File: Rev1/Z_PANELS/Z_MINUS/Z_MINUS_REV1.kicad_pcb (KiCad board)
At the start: 2 copper layers, 98 x 98 mm, 57 parts, among them IC1 LTC4316IDD#PBF, IC2 SM141K08TFV, IC3 SM141K04TFV, IC4 SM141K04TFV, IC5 SM141K04TFV, IC6 SM141K08TFV, J1 F3311A7H121014E200, Q1 BSS138, Q2 BSS138, Q3 MBT2222ADW1T1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

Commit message: fixed bugs and finished Z plus
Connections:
- JP2 pad 3: /SUN_SENSOR/+3.3v -> +3.3V
- U1 pad 1: /SUN_SENSOR/+3.3v -> +3.3V
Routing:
- net +3.3V: track 144.2 -> 157.6 mm
- net /SUN_SENSOR/+3.3v: track 2.25 -> 0.00 mm

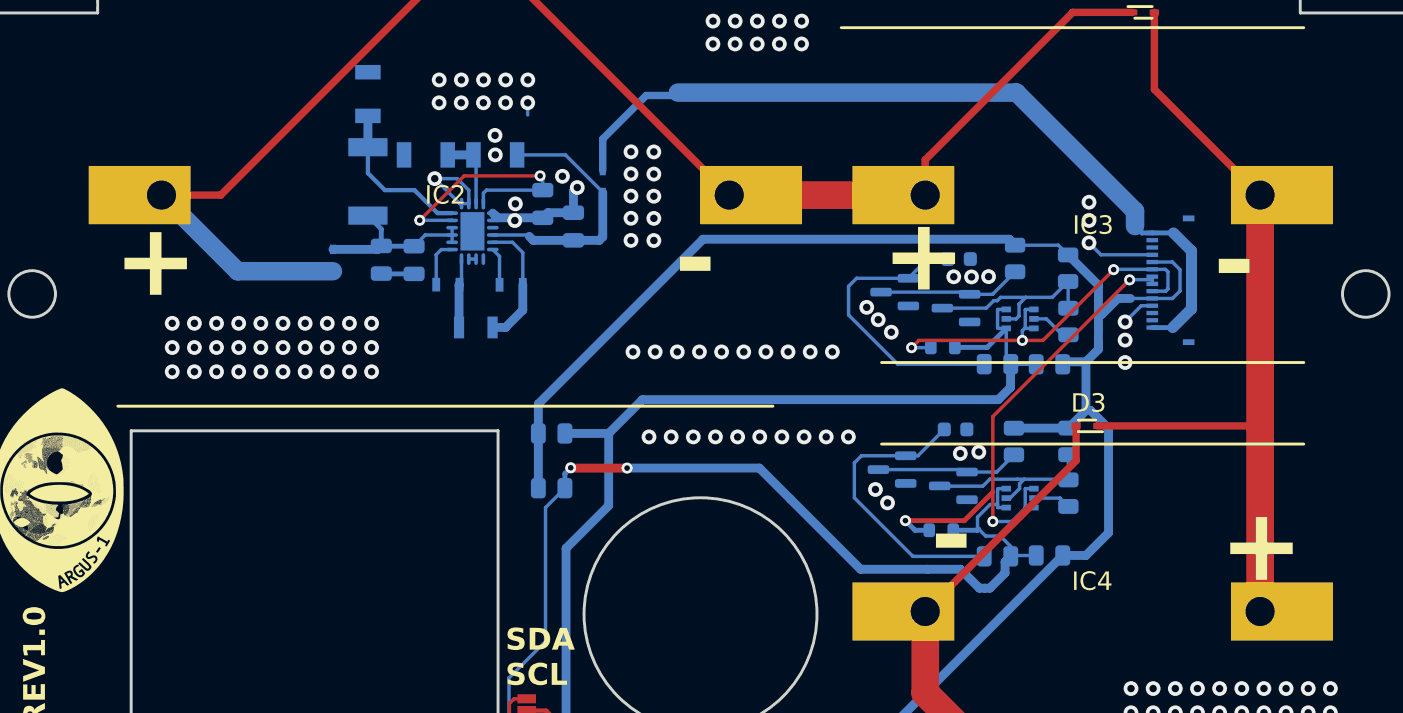
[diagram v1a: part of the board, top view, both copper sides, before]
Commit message: CHANGED Resistor values for MPPC; added testpoints and silkscreen info
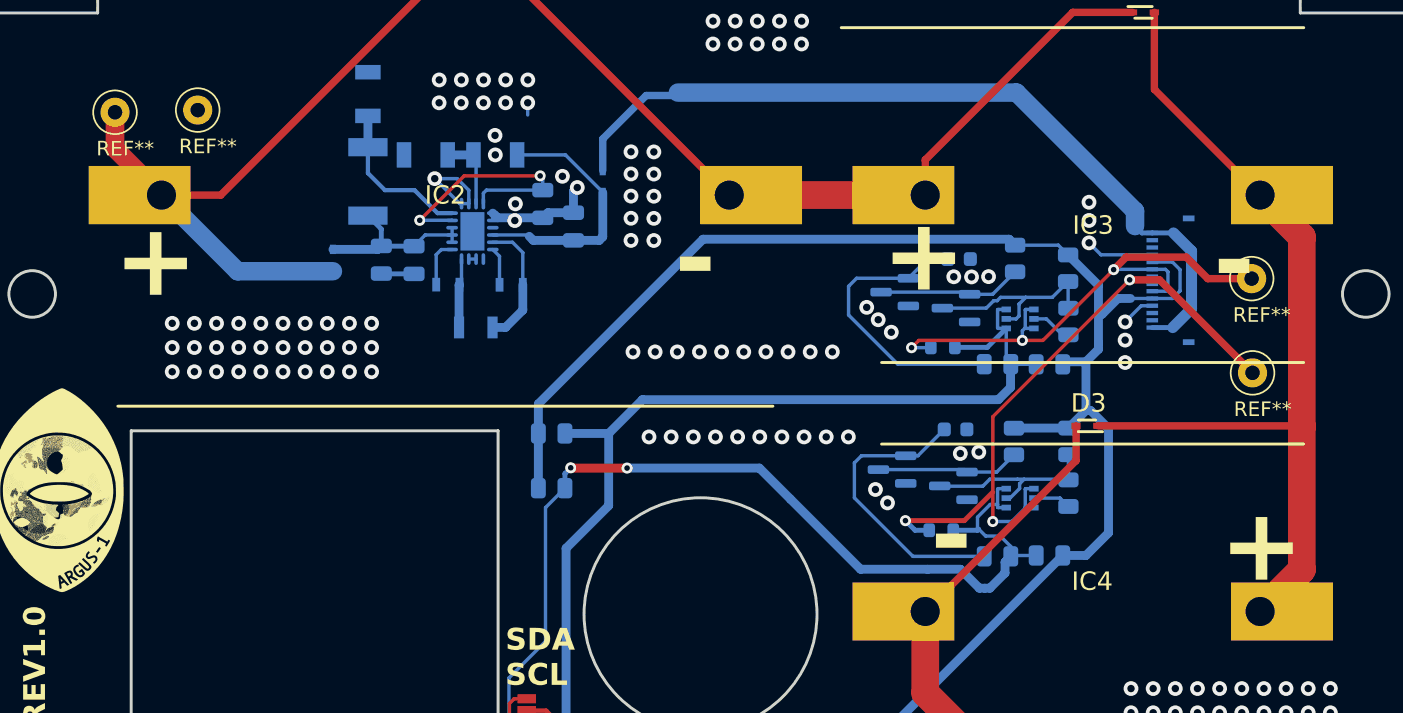
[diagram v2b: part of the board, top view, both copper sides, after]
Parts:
- added REF**: TestPoint_Loop_D2.50mm_Drill1.0mm, TestPoint:TestPoint_Loop_D2.50mm_Drill1.0mm, F.Cu at (102.0, 67.0)
- added REF**: TestPoint_Loop_D2.50mm_Drill1.0mm, TestPoint:TestPoint_Loop_D2.50mm_Drill1.0mm, F.Cu at (174.5, 85.0)
- added REF**: TestPoint_Loop_D2.50mm_Drill1.0mm, TestPoint:TestPoint_Loop_D2.50mm_Drill1.0mm, F.Cu at (96.3, 67.1)
- added REF**: TestPoint_Loop_D2.50mm_Drill1.0mm, TestPoint:TestPoint_Loop_D2.50mm_Drill1.0mm, F.Cu at (174.4, 78.5)
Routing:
- net SDA1_b4iso: track 36.4 -> 47.5 mm
- net SCL1_b4iso: track 26.9 -> 37.4 mm
- net /SOLAR_PANEL_ELECTRONICS/7023_vout: track 41.5 -> 48.5 mm
- net Net-(IC3-NEG): track 55.3 -> 60.6 mm
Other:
- board text added: "PANEL+"
- board text added: "PANEL-"
- board text added: "R19=14*R20"
- board text added: "TP1:SCL_BISO"
- board text added: "TP2:SDA_BSIO"

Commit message: updated boards
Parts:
- removed the C3 at (114.6, 77.2)
- removed the C4 at (116.9, 77.3)
- removed R21: RV1206JR-0722ML, AA_AUTO_LOADER:RESC3116X65N
- removed R22: RC1206FR-072ML, AA_AUTO_LOADER:RESC3116X65N
- removed REF** (x4): TestPoint_Loop_D2.50mm_Drill1.0mm, TestPoint:TestPoint_Loop_D2.50mm_Drill1.0mm
- added C1: 0.1uF, Capacitor_SMD:C_0805_2012Metric, F.Cu at (128.6, 113.3)
- added C10: CGA3E2X7R1H223K080AA, AA_AUTO_LOADER:CAPC1608X90N, B.Cu at (70.5, 76.2)
- added C11: 47uF, Capacitor_SMD:C_0805_2012Metric, B.Cu at (74.4, 86.4)
- added C2: 0.1uF, Capacitor_SMD:C_0805_2012Metric, B.Cu at (64.5, 77.3)
- added C9: CGA3E2X7R1H223K080AA, AA_AUTO_LOADER:CAPC1608X90N, B.Cu at (118.0, 81.8)
- C6: value CGA3E2X7R1H223K080AA -> 47uF; footprint AA_AUTO_LOADER:CAPC1608X90N -> Capacitor_SMD:C_0805_2012Metric
- C7: value CGA3E2X7R1H223K080AA -> 1uF; footprint AA_AUTO_LOADER:CAPC1608X90N -> Capacitor_SMD:C_0805_2012Metric
- D1, D2, D3, D5, D6: value RB521S30T1G -> LSM115JE3_TR13; footprint AA_AUTO_LOADER:SODFL1608X70N -> AA_AUTO_LOADER:DIOM5436X330N; moved to B.Cu
- D4, D7: value RB521S30T1G -> LSM115JE3_TR13; footprint AA_AUTO_LOADER:SODFL1608X70N -> AA_AUTO_LOADER:DIOM5436X330N
- R19: value CHV2010-FX-1005ELF -> 12M; moved to F.Cu
- R20: value RC1206FR-072M49L -> 1M
- moved D5 90.9 mm to (119.4, 65.2), turned to 0 degrees
- moved D1 73.5 mm to (130.8, 129.8), turned to 180 degrees
- moved D2 69.9 mm to (163.9, 130.1), turned to 180 degrees
- moved D6 69.2 mm to (107.1, 78.1)
- moved R20 56.2 mm to (73.9, 105.5), turned to 180 degrees
- moved C8 54.1 mm to (74.4, 83.3), turned to 180 degrees
- moved L1 51.3 mm to (73.6, 101.3)
- moved C5 51.3 mm to (74.4, 74.3), turned to 180 degrees
- moved C7 49.2 mm to (74.4, 80.3)
- moved D4 48.1 mm to (158.9, 70.3), turned to 0 degrees
- moved C6 44.8 mm to (74.4, 77.3)
- moved D3 14.5 mm to (160.2, 102.9)
- moved D7 5.61 mm to (130.6, 66.3), turned to 180 degrees
- moved R19 2.70 mm to (111.0, 72.0)
- moved U2 0.13 mm to (120.8, 75.3)
- renumbered C1 to C3, C2 to C4, IC6 to IC2, IC5 to IC3, IC3 to IC5, IC2 to IC6
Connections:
- C5 pad 1: Net-(U2-VCC) -> Net-(U2-PVIN)
- C6 pad 1: Net-(U2-SW1) -> Net-(U2-PVIN)
- C6 pad 2: Net-(U2-BST1) -> GND
- C7 pad 1: Net-(U2-SW2) -> Net-(U2-PVIN)
- C7 pad 2: Net-(U2-BST2) -> GND
- C8 pad 1: Net-(U2-VOUT) -> Net-(U2-VCC)
- D1 pad 1: /SOLAR_PANEL_ELECTRONICS/7023_vout -> Net-(IC2-POS)
- D1 pad 2: Net-(IC2-NEG) -> GND
- D2 pad 1: Net-(IC2-NEG) -> Net-(IC3-POS)
- D2 pad 2: Net-(IC3-NEG) -> Net-(IC2-POS)
- D3 pad 1: Net-(IC3-NEG) -> Net-(IC4-POS)
- D3 pad 2: Net-(IC4-NEG) -> Net-(IC3-POS)
- D4 pad 1: Net-(U2-PVIN) -> Net-(IC5-POS)
- D4 pad 2: /SOLAR_PANEL_ELECTRONICS/7023_vout -> Net-(IC4-POS)
- D5 pad 1: Net-(IC4-NEG) -> /SOLAR_PANEL_ELECTRONICS/7023_vout
- D5 pad 2: Net-(IC5-NEG) -> Net-(IC5-POS)
- D6 pad 1: Net-(IC5-NEG) -> Net-(U2-PVIN)
- D6 pad 2: GND -> /SOLAR_PANEL_ELECTRONICS/7023_vout
- IC2 pad 1: Net-(IC5-NEG) -> Net-(IC2-POS)
- IC3 pad 1: Net-(IC4-NEG) -> Net-(IC3-POS)
- IC3 pad 2: Net-(IC5-NEG) -> Net-(IC2-POS)
- IC4 pad 1: Net-(IC3-NEG) -> Net-(IC4-POS)
- IC4 pad 2: Net-(IC4-NEG) -> Net-(IC3-POS)
- IC5 pad 1: Net-(IC2-NEG) -> Net-(IC5-POS)
- IC5 pad 2: Net-(IC3-NEG) -> Net-(IC4-POS)
- IC6 pad 2: Net-(IC2-NEG) -> Net-(IC5-POS)
- U2 pad 9: /SOLAR_PANEL_ELECTRONICS/FB1 -> Net-(U2-VCC)
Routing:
- net Net-(IC4-NEG): track 72.9 -> 0.00 mm
- net Net-(IC3-NEG): track 60.6 -> 0.00 mm
- net Net-(IC4-POS): track 0.00 -> 59.0 mm
- net Net-(IC2-NEG): track 57.5 -> 0.00 mm
- net Net-(IC5-NEG): track 55.7 -> 0.00 mm
- net Net-(IC3-POS): track 0.00 -> 53.6 mm
- net /SOLAR_PANEL_ELECTRONICS/7023_vout: track 48.5 -> 7.53 mm
- net Net-(IC2-POS): track 0.00 -> 28.9 mm
- net GND: track 62.1 -> 34.0 mm, vias 253 -> 243
- net VSOLAR: track 56.2 -> 80.6 mm
- net Net-(IC5-POS): track 0.00 -> 19.2 mm
- net SDA1_b4iso: track 47.5 -> 36.4 mm
- net Net-(U2-PVIN): track 12.1 -> 1.00 mm
- net SCL1_b4iso: track 37.4 -> 26.9 mm
- net +3.3V: track 157.6 -> 165.6 mm
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
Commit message: generated ibom
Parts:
- R19: moved to B.Cu
- moved L1 57.3 mm to (119.6, 67.2), turned to 0 degrees
- moved C5 53.8 mm to (128.1, 72.1), turned to -90 degrees
- moved C6 50.7 mm to (125.0, 73.8), turned to -90 degrees
- moved C7 48.9 mm to (123.0, 74.5), turned to -90 degrees
- moved R20 48.6 mm to (108.1, 71.1), turned to 90 degrees
- moved C10 47.0 mm to (117.0, 69.8), turned to 0 degrees
- moved C11 43.1 mm to (113.9, 69.0), turned to 90 degrees
- moved C8 42.7 mm to (116.8, 77.8)
- moved D5 16.9 mm to (124.5, 81.3)
- moved C9 12.6 mm to (122.2, 69.9), turned to 0 degrees
- moved U2 3.04 mm to (118.5, 73.2)
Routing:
- net /SOLAR_PANEL_ELECTRONICS/7023_vout: track 7.53 -> 26.3 mm
- net Net-(U2-VOUT): track 17.8 -> 0.00 mm
- net GND: track 34.0 -> 16.5 mm, vias 243 -> 234
- net Net-(IC5-POS): track 19.2 -> 34.6 mm
- net Net-(U2-VCC): track 22.9 -> 9.53 mm, vias 2 -> 0
- net /SOLAR_PANEL_ELECTRONICS/MPPC1: track 10.9 -> 0.00 mm
- net Net-(U2-SW2): track 8.88 -> 0.00 mm
- net Net-(U2-SW1): track 4.77 -> 0.00 mm
- net Net-(U2-BST1): track 3.30 -> 0.00 mm
- net Net-(U2-BST2): track 2.61 -> 0.00 mm
- net Net-(U2-PVIN): track 1.00 -> 0.00 mm

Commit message: Z minus done
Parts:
- moved C2 77.2 mm to (129.7, 118.7)
- moved C5 19.9 mm to (108.3, 72.9), turned to 90 degrees
- moved C6 14.6 mm to (110.4, 72.9), turned to 90 degrees
- moved L1 12.2 mm to (117.5, 79.2), turned to 180 degrees
- moved R19 11.3 mm to (118.8, 63.8), turned to 0 degrees
- moved R20 10.7 mm to (117.9, 66.7), turned to 180 degrees
- moved C7 10.6 mm to (112.5, 72.9), turned to 90 degrees
- moved C11 10.4 mm to (123.3, 73.4), turned to -90 degrees
- moved C9 9.84 mm to (114.9, 76.5), turned to 180 degrees
- moved C8 8.60 mm to (121.3, 70.5), turned to 0 degrees
- moved C10 7.45 mm to (120.1, 76.6), turned to 180 degrees
- moved U2 0.85 mm to (117.7, 73.3)
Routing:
- net Net-(U2-PVIN): track 0.00 -> 47.9 mm
- net GND: track 16.5 -> 36.4 mm, vias 234 -> 233
- net Net-(U2-VOUT): track 0.00 -> 12.9 mm
- net /SOLAR_PANEL_ELECTRONICS/MPPC1: track 0.00 -> 10.4 mm, vias 0 -> 2
- net Net-(U2-SW2): track 0.00 -> 7.62 mm
- net Net-(U2-VCC): track 9.53 -> 17.2 mm
- net Net-(U2-SW1): track 0.00 -> 4.96 mm
- net Net-(U2-BST1): track 0.00 -> 3.51 mm
- net +3.3V: track 165.6 -> 167.7 mm
- net /SOLAR_PANEL_ELECTRONICS/7023_vout: track 26.3 -> 28.4 mm
- net Net-(U2-BST2): track 0.00 -> 2.11 mm

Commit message: SIGNOFF:NISCHAL Z MINUS
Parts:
- added ?: , , F.Cu at (99.0, 123.9)
- added ?: , , F.Cu at (98.4, 66.0)
- added ?: , , F.Cu at (174.7, 87.2)
- added REF**: Test_Point_D1.02mm, digikey-footprints:Test_Point_D1.02mm, F.Cu at (169.7, 87.6)
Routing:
- net SDA1_b4iso: track 36.4 -> 52.5 mm
- net SCL1_b4iso: track 26.9 -> 42.8 mm
- net /SOLAR_PANEL_ELECTRONICS/7023_vout: track 28.4 -> 35.6 mm
